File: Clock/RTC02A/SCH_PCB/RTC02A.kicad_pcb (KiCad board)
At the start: 2 copper layers, 50.8 x 42.2 mm, 20 parts, among them J1 JUMP_5X2, J2 JUMP2_2x1, J3 JUMP_2x1, J4 JUMP_2x1, J5 JUMP_2x1, M1 HOLE, M2 HOLE, M3 HOLE, M4 HOLE, SW1 SW_PUSH, U1 PCF85263A, Y1 ABS07-120-32.768KHZ-T

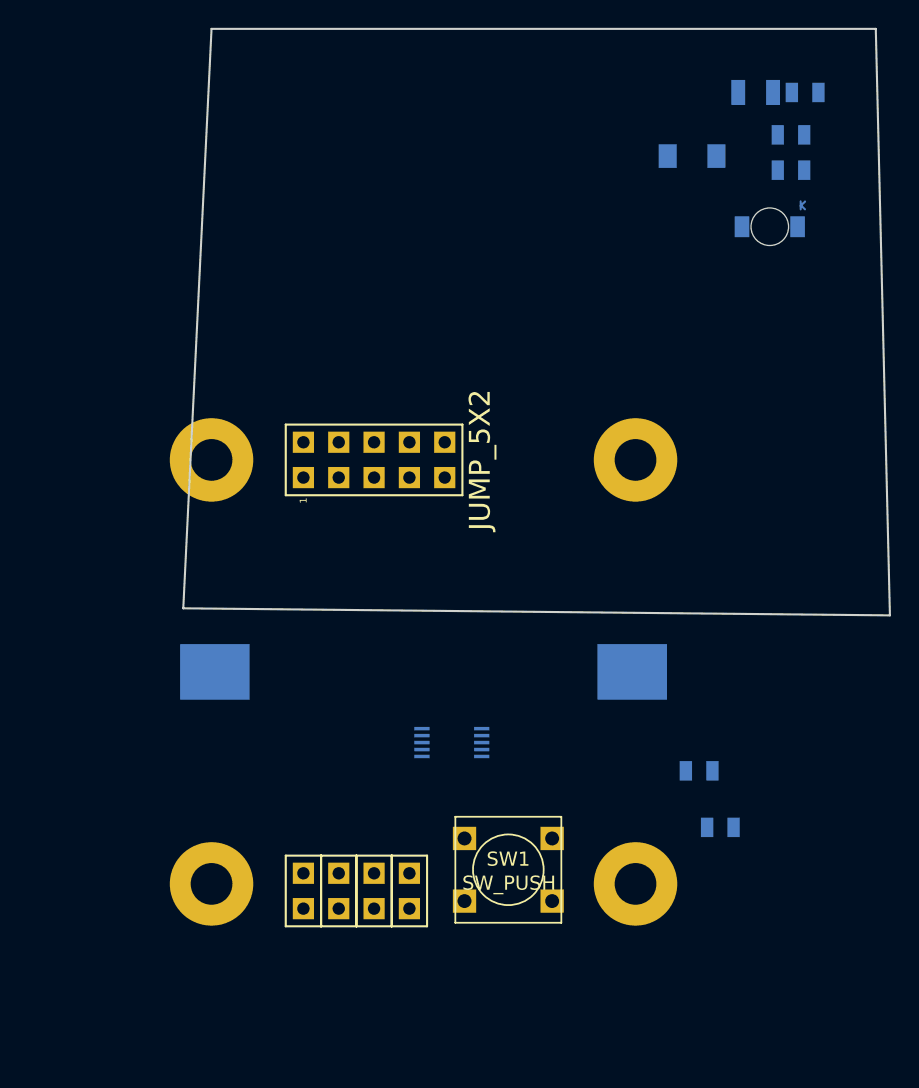
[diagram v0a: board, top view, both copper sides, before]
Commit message: 
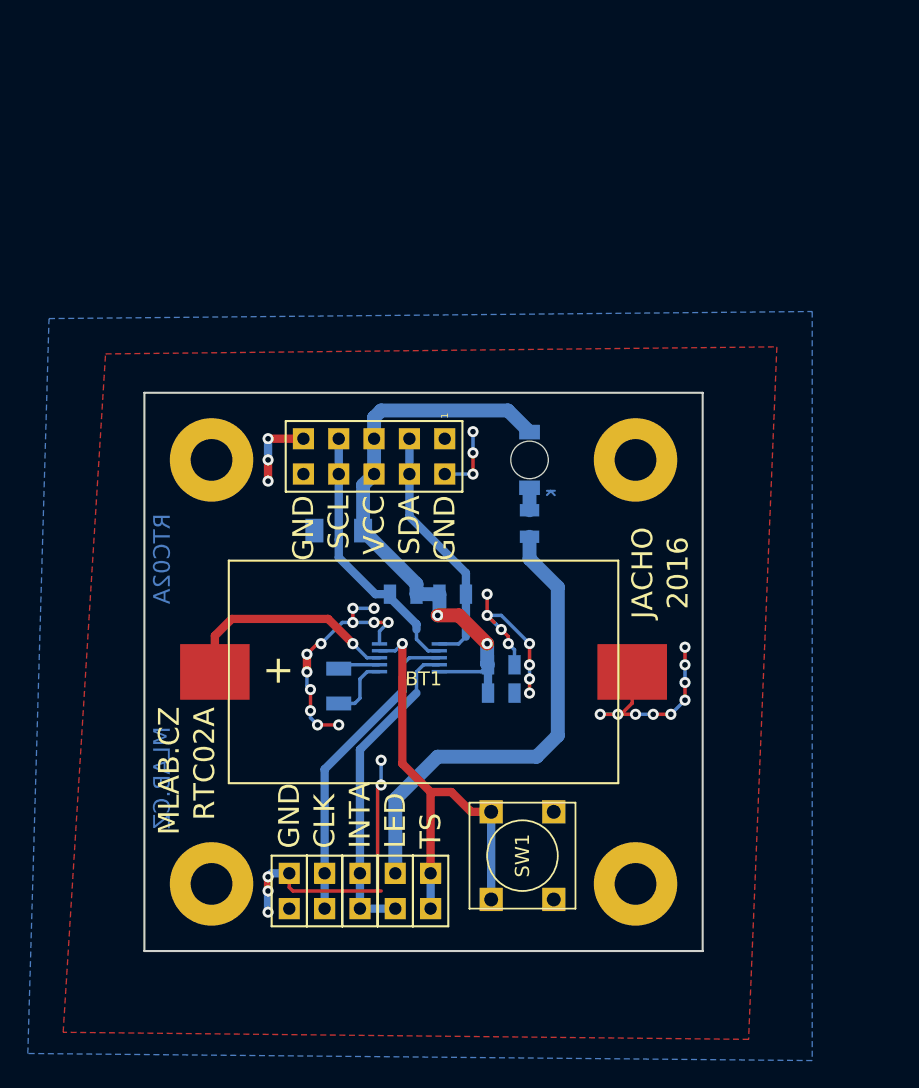
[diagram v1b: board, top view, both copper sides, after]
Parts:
- added J6: JUMP_2x1, Mlab_Pin_Headers:Straight_2x01, F.Cu at (10.7, -4.57)
- BT1: moved to F.Cu
- moved Y1 52.1 mm to (14.2, -19.3), turned to 90 degrees
- moved C2 45.2 mm to (25.9, -18.8)
- moved C1 41.2 mm to (25.9, -20.8)
- moved D1 37.0 mm to (14.2, -30.5)
- moved R1 36.8 mm to (27.9, -31.0), turned to 270 degrees
- moved R3 25.5 mm to (22.4, -25.9)
- moved R2 24.8 mm to (18.9, -25.9), turned to 180 degrees
- moved D2 24.1 mm to (27.9, -35.6), turned to 270 degrees
- moved U1 6.82 mm to (19.3, -21.3)
- moved J2 4.06 mm to (18.3, -4.57)
- moved J4 1.52 mm to (13.2, -4.57)
- moved J5 1.52 mm to (20.8, -4.57)
- moved SW1 1.44 mm to (27.4, -7.11), turned to 90 degrees
- moved J3 1.02 mm to (15.7, -4.57)
- moved J1 0.25 mm to (16.8, -35.8), turned to 270 degrees
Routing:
- net GND: track 0.00 -> 81.4 mm, vias 0 -> 40
- net VCC: track 0.00 -> 41.5 mm, vias 0 -> 2
- net Net-(J2-Pad2): track 0.00 -> 34.0 mm
- net /TS: track 0.00 -> 33.0 mm, vias 0 -> 1
- net /INTA: track 0.00 -> 23.1 mm
- net /CLK: track 0.00 -> 22.7 mm
- net /SCL: track 0.00 -> 19.3 mm
- net /SDA: track 0.00 -> 18.0 mm
- net Net-(BT1-Pad1): track 0.00 -> 16.1 mm, vias 0 -> 1
- net Net-(U1-Pad1): track 0.00 -> 4.69 mm
- net Net-(U1-Pad2): track 0.00 -> 3.05 mm
- net Net-(D2-Pad1): track 0.00 -> 1.57 mm
- added copper zone on B.Cu, net GND
- added copper zone on F.Cu, net GND
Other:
- board size 50.8 x 42.2 mm -> 40.1 x 40.1 mm
- net class Default: trace_width 0.25 -> 0.2; via_dia 0.6 -> 0.8
- board text added: "2016"
- board text added: "CLK"
- board text added: "GND"
- board text added: "INTA"
- board text added: "JACHO"
- board text added: "LED"
- board text added: "MLAB.CZ"
- board text added: "RTC02A"
- board text added: "SCL"
- board text added: "SDA"
- board text added: "TS"
- board text added: "VCC"
